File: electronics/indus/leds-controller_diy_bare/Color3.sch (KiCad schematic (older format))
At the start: 20 parts, among them Q4 Q_NPN_BCE, U2 TPS92513

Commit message: footprint with libraries
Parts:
- removed Q4: Q_NPN_BCE, symbol Q_NPN_BCE
- removed R13: R, symbol R
- C23, C6, C9: footprint (none) -> Capacitors_SMD:C_1206
- C7, C8: footprint (none) -> Capacitors_SMD:C_0805
- D5: footprint (none) -> Diodes_SMD:SOD-123
- R14, R20, R21: footprint (none) -> Resistors_SMD:R_0805
- R22: value R -> 1k; footprint (none) -> Resistors_SMD:R_0805
- R23: footprint (none) -> Resistors_SMD:R_1206
- U2: value TPS92513 -> TPS92513HVDGQT; footprint (none) -> risebox:BUCK_TPS92513_PowerPAD
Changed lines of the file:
@@
 P 5900 3950
 F 0 "U2" H 6250 3000 60  0000 C CNN
-F 1 "TPS92513" H 5500 3000 60  0000 C CNN
-F 2 "" H 6050 4050 60  0000 C CNN
+F 1 "TPS92513HVDGQT" H 5500 3000 60  0000 C CNN
+F 2 "risebox:BUCK_TPS92513_PowerPAD" H 6050 4050 60  0001 C CNN
 F 3 "" H 6050 4050 60  0000 C CNN
 	1    5900 3950
@@
 F 0 "C6" H 1750 4650 40  0000 L CNN
 F 1 "4.7µF" H 1756 4465 40  0000 L CNN
-F 2 "" H 1788 4400 30  0000 C CNN
+F 2 "Capacitors_SMD:C_1206" H 1788 4400 30  0001 C CNN
 F 3 "" H 1750 4550 60  0000 C CNN
 	1    1750 4550
@@
 $EndComp
 $Comp
-L GND-RESCUE-leds-controller #PWR13
+L GND-RESCUE-leds-controller #PWR014
 U 1 1 5766F8ED
 P 6050 5650
-F 0 "#PWR13" H 6050 5650 30  0001 C CNN
+F 0 "#PWR014" H 6050 5650 30  0001 C CNN
 F 1 "GND" H 6050 5580 30  0001 C CNN
 F 2 "" H 6050 5650 60  0000 C CNN
@@
 F 0 "R14" V 3730 4200 40  0000 C CNN
 F 1 "176k" V 3657 4201 40  0000 C CNN
-F 2 "" V 3580 4200 30  0000 C CNN
+F 2 "Resistors_SMD:R_0805" V 3580 4200 30  0001 C CNN
 F 3 "" H 3650 4200 30  0000 C CNN
 	1    3650 4200
@@
 F 0 "R20" V 3730 4900 40  0000 C CNN
 F 1 "19.3k" V 3657 4901 40  0000 C CNN
-F 2 "" V 3580 4900 30  0000 C CNN
+F 2 "Resistors_SMD:R_0805" V 3580 4900 30  0001 C CNN
 F 3 "" H 3650 4900 30  0000 C CNN
 	1    3650 4900
@@
 F 0 "C7" H 4400 4950 40  0000 L CNN
 F 1 "0.1µF" H 4406 4765 40  0000 L CNN
-F 2 "" H 4438 4700 30  0000 C CNN
+F 2 "Capacitors_SMD:C_0805" H 4438 4700 30  0001 C CNN
 F 3 "" H 4400 4850 60  0000 C CNN
 	1    4400 4850
@@
 F 0 "R21" V 5030 4900 40  0000 C CNN
 F 1 "200k" V 4957 4901 40  0000 C CNN
-F 2 "" V 4880 4900 30  0000 C CNN
+F 2 "Resistors_SMD:R_0805" V 4880 4900 30  0001 C CNN
 F 3 "" H 4950 4900 30  0000 C CNN
 	1    4950 4900
@@
 F 0 "C8" H 6900 3400 40  0000 L CNN
 F 1 "0.1µF" H 6906 3215 40  0000 L CNN
-F 2 "" H 6938 3150 30  0000 C CNN
+F 2 "Capacitors_SMD:C_0805" H 6938 3150 30  0001 C CNN
 F 3 "" H 6900 3300 60  0000 C CNN
 	1    6900 3300
@@
 F 0 "C9" H 9650 4250 40  0000 L CNN
 F 1 "4.7µF" H 9656 4065 40  0000 L CNN
-F 2 "" H 9688 4000 30  0000 C CNN
+F 2 "Capacitors_SMD:C_1206" H 9688 4000 30  0001 C CNN
 F 3 "" H 9650 4150 60  0000 C CNN
 	1    9650 4150
@@
 P 8300 4450
 F 0 "R22" V 8380 4450 40  0000 C CNN
-F 1 "R" V 8307 4451 40  0000 C CNN
-F 2 "" V 8230 4450 30  0000 C CNN
+F 1 "1k" V 8307 4451 40  0000 C CNN
+F 2 "Resistors_SMD:R_0805" V 8230 4450 30  0001 C CNN
 F 3 "" H 8300 4450 30  0000 C CNN
 	1    8300 4450
@@
 F 0 "R23" V 10330 4900 40  0000 C CNN
 F 1 "0.2" V 10257 4901 40  0000 C CNN
-F 2 "" V 10180 4900 30  0000 C CNN
+F 2 "Resistors_SMD:R_1206" V 10180 4900 30  0001 C CNN
 F 3 "" H 10250 4900 30  0000 C CNN
 	1    10250 4900
@@
 F 0 "D5" H 7450 5000 40  0000 C CNN
 F 1 "DIODESCH" H 7450 4800 40  0000 C CNN
-F 2 "" H 7450 4900 60  0000 C CNN
+F 2 "Diodes_SMD:SOD-123" H 7450 4900 60  0001 C CNN
 F 3 "" H 7450 4900 60  0000 C CNN
 	1    7450 4900
@@
 F 0 "JP11" H 2500 1550 50  0000 C CNN
 F 1 "JUMPER" H 2500 1320 50  0000 C CNN
-F 2 "" H 2500 1400 50  0000 C CNN
+F 2 "" H 2500 1400 50  0001 C CNN
 F 3 "" H 2500 1400 50  0000 C CNN
 	1    2500 1400
@@
 F 0 "JP12" H 2500 1900 50  0000 C CNN
 F 1 "JUMPER" H 2500 1670 50  0000 C CNN
-F 2 "" H 2500 1750 50  0000 C CNN
+F 2 "" H 2500 1750 50  0001 C CNN
 F 3 "" H 2500 1750 50  0000 C CNN
 	1    2500 1750
@@
 F 0 "JP13" H 2500 2250 50  0000 C CNN
 F 1 "JUMPER" H 2500 2020 50  0000 C CNN
-F 2 "" H 2500 2100 50  0000 C CNN
+F 2 "" H 2500 2100 50  0001 C CNN
 F 3 "" H 2500 2100 50  0000 C CNN
 	1    2500 2100
@@
 F 0 "JP14" H 2500 2600 50  0000 C CNN
 F 1 "JUMPER" H 2500 2370 50  0000 C CNN
-F 2 "" H 2500 2450 50  0000 C CNN
+F 2 "" H 2500 2450 50  0001 C CNN
 F 3 "" H 2500 2450 50  0000 C CNN
 	1    2500 2450
@@
 F 0 "JP15" H 5750 2000 50  0000 C CNN
 F 1 "JUMPER" H 5750 1770 50  0000 C CNN
-F 2 "" H 5750 1850 50  0000 C CNN
+F 2 "" H 5750 1850 50  0001 C CNN
 F 3 "" H 5750 1850 50  0000 C CNN
 	1    5750 1850
@@
 Connection ~ 3650 5300
 Wire Wire Line
-	2950 4700 2950 4550
-Wire Wire Line
-	2950 4550 3950 4550
-Wire Wire Line
-	2950 5100 2950 5200
-Wire Wire Line
-	2950 5200 3650 5200
-Connection ~ 3650 5200
-$Comp
-L Q_NPN_BCE Q4
-U 1 1 5766F9C8
-P 2850 4900
-F 0 "Q4" H 3150 4950 50  0000 R CNN
-F 1 "Q_NPN_BCE" H 3450 4850 50  0000 R CNN
-F 2 "" H 3050 5000 50  0000 C CNN
-F 3 "" H 2850 4900 50  0000 C CNN
-	1    2850 4900
-	1    0    0    -1
-$EndComp
-Text HLabel 1200 4900 0    60   Input ~ 0
-THERM_OFF
-$Comp
-L R R13
-U 1 1 5766F9D0
-P 2300 4900
-F 0 "R13" V 2380 4900 50  0000 C CNN
-F 1 "R" V 2300 4900 50  0000 C CNN
-F 2 "" V 2230 4900 50  0000 C CNN
-F 3 "" H 2300 4900 50  0000 C CNN
-	1    2300 4900
-	0    1    1    0
-$EndComp
-Wire Wire Line
-	2450 4900 2650 4900
-Wire Wire Line
-	2150 4900 1200 4900
+	3650 4550 3950 4550
 $Comp
 L C C23
@@
 F 0 "C23" H 2075 4650 50  0000 L CNN
 F 1 "4.7µF" H 2075 4450 50  0000 L CNN
-F 2 "" H 2088 4400 50  0000 C CNN
+F 2 "Capacitors_SMD:C_1206" H 2088 4400 50  0001 C CNN
 F 3 "" H 2050 4550 50  0000 C CNN
 	1    2050 4550

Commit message: fix some errors
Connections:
- net VIN: now also U2.2 (VIN)
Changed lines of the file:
@@
 POT_OUT
 Wire Wire Line
-	1200 3850 5400 3850
+	1200 3850 5350 3850
 Wire Wire Line
 	1750 5300 10250 5300
@@
 	3650 5150 3650 5300
 Wire Wire Line
-	3650 3950 3650 3850
-Connection ~ 3650 3850
+	3650 3950 3600 3850
+Connection ~ 3600 3850
 Connection ~ 3650 5300
 Wire Wire Line

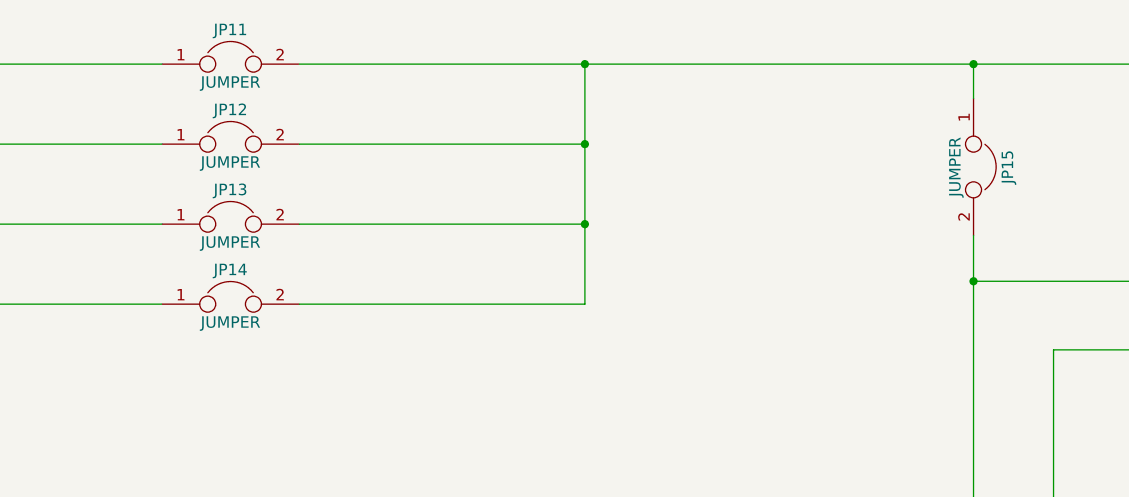
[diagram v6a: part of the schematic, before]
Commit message: add pinhead footprint
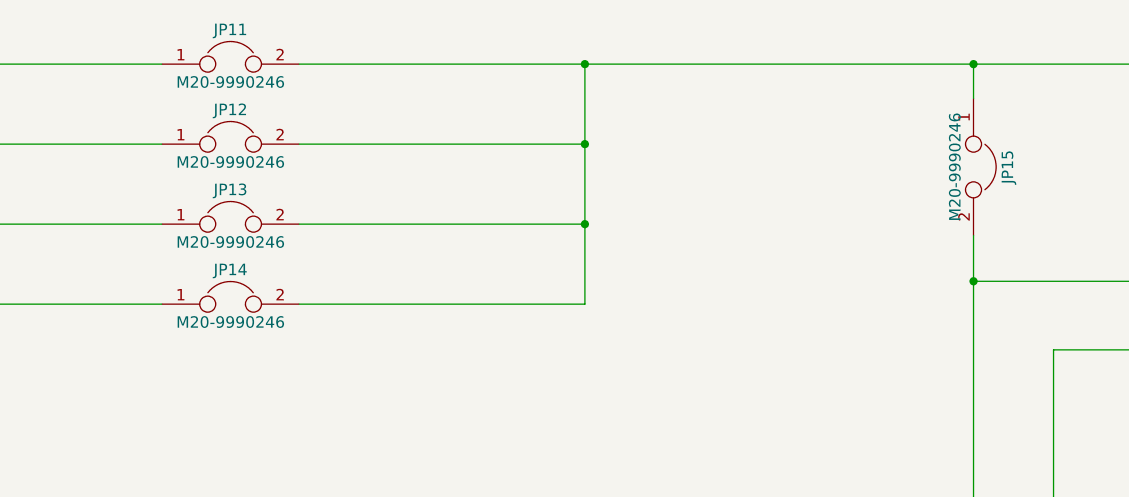
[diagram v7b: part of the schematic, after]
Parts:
- JP11, JP12, JP13, JP14, JP15: value JUMPER -> M20-9990246; footprint (none) -> Connect:PINHEAD1-2
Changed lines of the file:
@@
 P 2500 1400
 F 0 "JP11" H 2500 1550 50  0000 C CNN
-F 1 "JUMPER" H 2500 1320 50  0000 C CNN
-F 2 "" H 2500 1400 50  0001 C CNN
+F 1 "M20-9990246" H 2500 1320 50  0000 C CNN
+F 2 "Connect:PINHEAD1-2" H 2500 1400 50  0001 C CNN
 F 3 "" H 2500 1400 50  0000 C CNN
 	1    2500 1400
@@
 P 2500 1750
 F 0 "JP12" H 2500 1900 50  0000 C CNN
-F 1 "JUMPER" H 2500 1670 50  0000 C CNN
-F 2 "" H 2500 1750 50  0001 C CNN
+F 1 "M20-9990246" H 2500 1670 50  0000 C CNN
+F 2 "Connect:PINHEAD1-2" H 2500 1750 50  0001 C CNN
 F 3 "" H 2500 1750 50  0000 C CNN
 	1    2500 1750
@@
 P 2500 2100
 F 0 "JP13" H 2500 2250 50  0000 C CNN
-F 1 "JUMPER" H 2500 2020 50  0000 C CNN
-F 2 "" H 2500 2100 50  0001 C CNN
+F 1 "M20-9990246" H 2500 2020 50  0000 C CNN
+F 2 "Connect:PINHEAD1-2" H 2500 2100 50  0001 C CNN
 F 3 "" H 2500 2100 50  0000 C CNN
 	1    2500 2100
@@
 P 2500 2450
 F 0 "JP14" H 2500 2600 50  0000 C CNN
-F 1 "JUMPER" H 2500 2370 50  0000 C CNN
-F 2 "" H 2500 2450 50  0001 C CNN
+F 1 "M20-9990246" H 2500 2370 50  0000 C CNN
+F 2 "Connect:PINHEAD1-2" H 2500 2450 50  0001 C CNN
 F 3 "" H 2500 2450 50  0000 C CNN
 	1    2500 2450
@@
 P 5750 1850
 F 0 "JP15" H 5750 2000 50  0000 C CNN
-F 1 "JUMPER" H 5750 1770 50  0000 C CNN
-F 2 "" H 5750 1850 50  0001 C CNN
+F 1 "M20-9990246" H 5750 1770 50  0000 C CNN
+F 2 "Connect:PINHEAD1-2" H 5750 1850 50  0001 C CNN
 F 3 "" H 5750 1850 50  0000 C CNN
 	1    5750 1850
